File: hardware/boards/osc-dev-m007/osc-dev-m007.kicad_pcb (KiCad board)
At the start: 4 copper layers, 1 part, among them U1 CH32M007E8U7

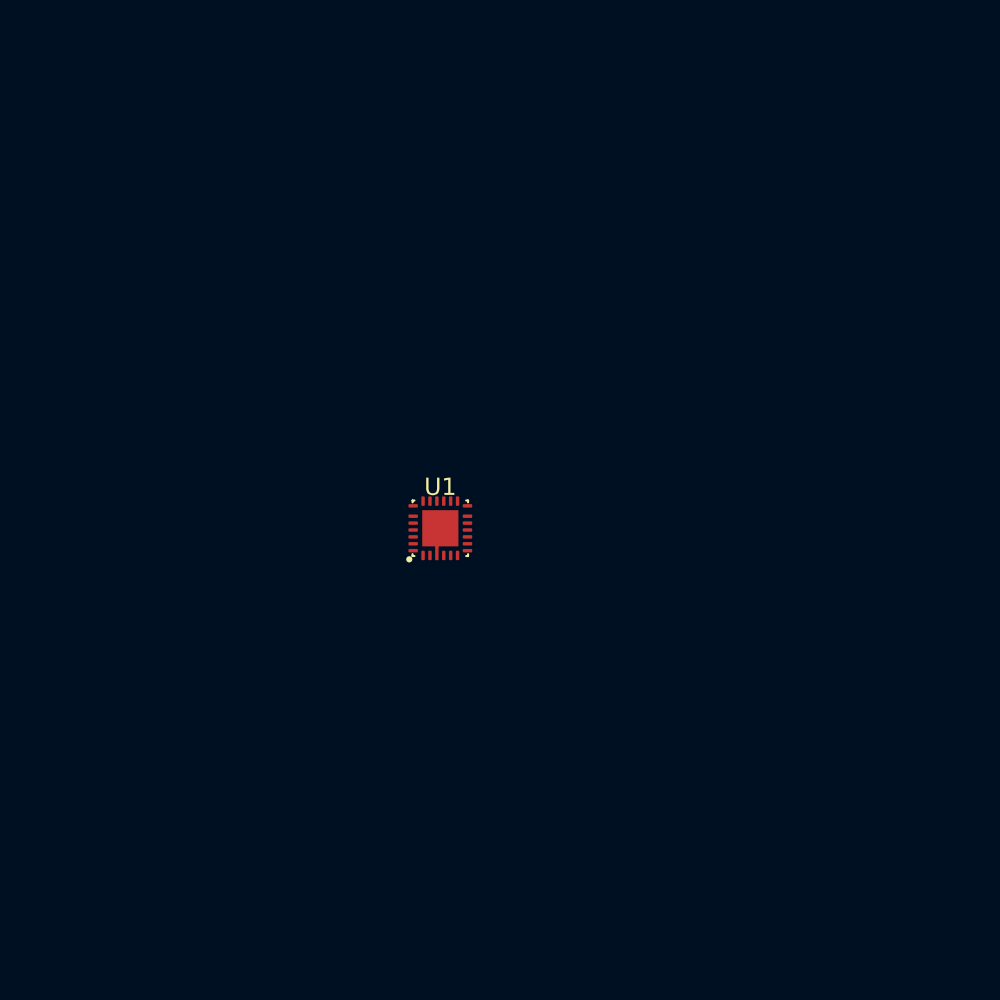
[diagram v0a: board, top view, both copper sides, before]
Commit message: hw: design osc-dev-m007 pcb
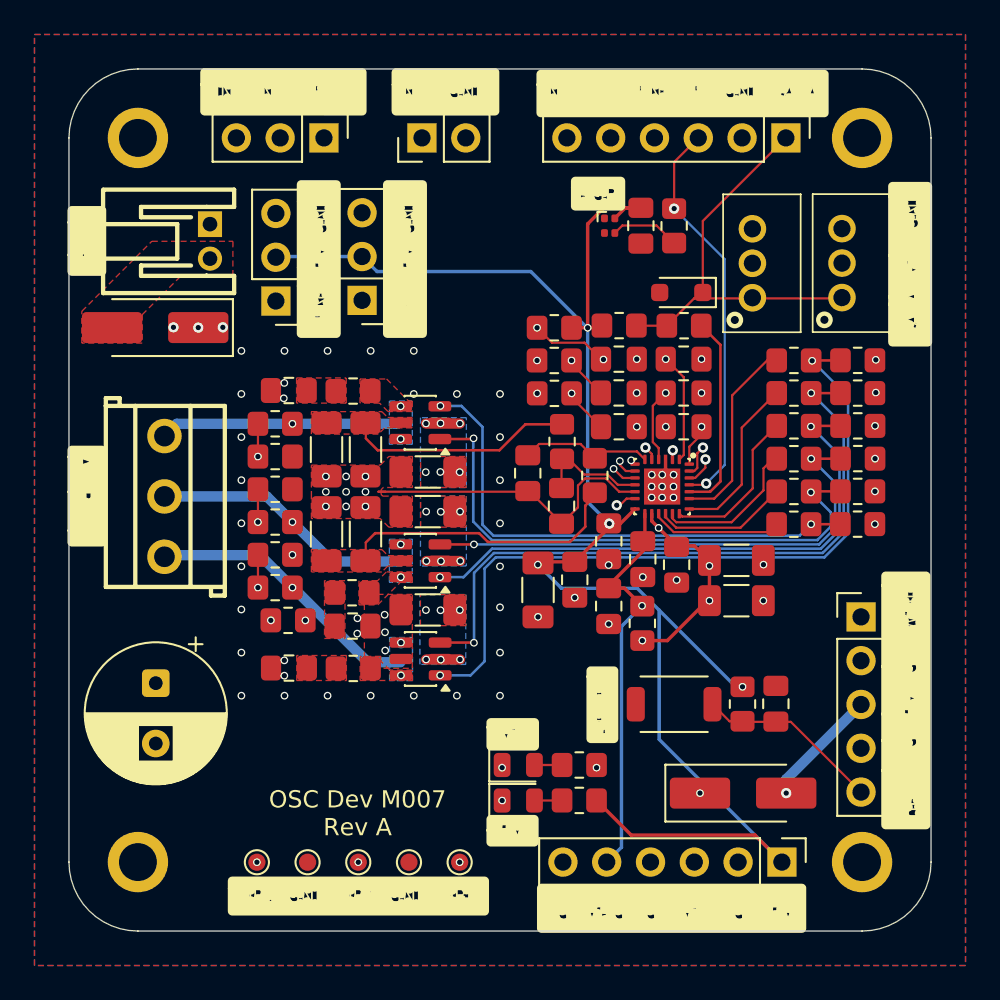
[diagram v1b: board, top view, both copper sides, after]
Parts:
- removed U1: CH32M007E8U7, shared:QFN-26_3x3mm_P0.4mm
- added C1001: 1nF, Capacitor_SMD:C_0805_2012Metric_Pad1.18x1.45mm_HandSolder, F.Cu at (157.0, 98.7)
- added C1002: 0.1µF, Capacitor_SMD:C_0805_2012Metric_Pad1.18x1.45mm_HandSolder, F.Cu at (157.0, 96.7)
- added C1003: 0.1µF, Capacitor_SMD:C_0805_2012Metric_Pad1.18x1.45mm_HandSolder, F.Cu at (157.0, 94.8)
- added C201: 2.2uF, Capacitor_SMD:C_0805_2012Metric_Pad1.18x1.45mm_HandSolder, F.Cu at (156.4, 109.1)
- added C202: 2.2uF, Capacitor_SMD:C_0805_2012Metric_Pad1.18x1.45mm_HandSolder, F.Cu at (158.3, 106.4)
- added C203: 0.1uF, Capacitor_SMD:C_0805_2012Metric_Pad1.18x1.45mm_HandSolder, F.Cu at (160.3, 106.7)
- added C204: 10uF, Capacitor_SMD:C_1206_3216Metric_Pad1.33x1.80mm_HandSolder, F.Cu at (163.8, 106.4)
- added C205: 10uF, Capacitor_SMD:C_1206_3216Metric_Pad1.33x1.80mm_HandSolder, F.Cu at (163.8, 108.8)
- added C206: 0.1uF, Capacitor_SMD:C_0805_2012Metric_Pad1.18x1.45mm_HandSolder, F.Cu at (156.4, 105.3)
- added C207: 1uF, Capacitor_SMD:C_0805_2012Metric_Pad1.18x1.45mm_HandSolder, F.Cu at (154.4, 107.5)
- added C208: 10uF, Capacitor_SMD:C_1206_3216Metric_Pad1.33x1.80mm_HandSolder, F.Cu at (152.3, 108.1)
- added C209: 0.1uF, Capacitor_SMD:C_0805_2012Metric_Pad1.18x1.45mm_HandSolder, F.Cu at (166.1, 114.7)
- added C210: 0.1uF, Capacitor_SMD:C_0805_2012Metric_Pad1.18x1.45mm_HandSolder, F.Cu at (158.2, 87.0)
- added C301: 470uF 25V, Capacitor_THT:CP_Radial_D8.0mm_P3.50mm, F.Cu at (130.1, 113.5)
- added C401: 10uF, Capacitor_SMD:C_1206_3216Metric_Pad1.33x1.80mm_HandSolder, F.Cu at (145.9, 101.3)
- added C402: 1nF, Capacitor_SMD:C_0805_2012Metric_Pad1.18x1.45mm_HandSolder, F.Cu at (160.7, 94.8)
- added C403: 1nF, Capacitor_SMD:C_0805_2012Metric_Pad1.18x1.45mm_HandSolder, F.Cu at (137.8, 96.6)
- added C501: 1nF, Capacitor_SMD:C_0805_2012Metric_Pad1.18x1.45mm_HandSolder, F.Cu at (153.6, 103.3)
- added C601: 10uF, Capacitor_SMD:C_1206_3216Metric_Pad1.33x1.80mm_HandSolder, F.Cu at (145.9, 103.6)
- added C602: 1nF, Capacitor_SMD:C_0805_2012Metric_Pad1.18x1.45mm_HandSolder, F.Cu at (160.7, 96.7)
- added C603: 1nF, Capacitor_SMD:C_0805_2012Metric_Pad1.18x1.45mm_HandSolder, F.Cu at (141.5, 110.2)
- added C701: 1nF, Capacitor_SMD:C_0805_2012Metric_Pad1.18x1.45mm_HandSolder, F.Cu at (151.7, 101.4)
- added C801: 10uF, Capacitor_SMD:C_1206_3216Metric_Pad1.33x1.80mm_HandSolder, F.Cu at (145.9, 109.3)
- added C802: 1nF, Capacitor_SMD:C_0805_2012Metric_Pad1.18x1.45mm_HandSolder, F.Cu at (160.7, 98.7)
- added C803: 1nF, Capacitor_SMD:C_0805_2012Metric_Pad1.18x1.45mm_HandSolder, F.Cu at (137.8, 112.7)
- added D1101: PESD5V0L1BA, Diode_SMD:D_SOD-323_HandSoldering, F.Cu at (160.6, 90.9)
- added D201: STAT, shared:LED_XL-1010RGBC-WS2812B_1x1mm, F.Cu at (156.4, 87.0)
- added D901: SS54, Diode_SMD:D_SMA_Handsoldering, F.Cu at (130.1, 92.9)
- added D902: SS54, Diode_SMD:D_SMA_Handsoldering, F.Cu at (164.2, 119.9)
- added H101: MountingHole_Pad_MP, MountingHole:MountingHole_2.2mm_M2_ISO7380_Pad, F.Cu at (129.1, 81.9)
- added H102: MountingHole_Pad_MP, MountingHole:MountingHole_2.2mm_M2_ISO7380_Pad, F.Cu at (129.1, 123.9)
- added H103: MountingHole_Pad_MP, MountingHole:MountingHole_2.2mm_M2_ISO7380_Pad, F.Cu at (171.1, 123.9)
- added H104: MountingHole_Pad_MP, MountingHole:MountingHole_2.2mm_M2_ISO7380_Pad, F.Cu at (171.1, 81.9)
- added J1001: NTC_EXT, Connector_PinHeader_2.54mm:PinHeader_1x02_P2.54mm_Vertical, F.Cu at (145.5, 81.9)
- added J1002: ENC, Connector_PinHeader_2.54mm:PinHeader_1x03_P2.54mm_Vertical, F.Cu at (137.1, 91.4)
- added J1003: POT, Connector_PinHeader_2.54mm:PinHeader_1x03_P2.54mm_Vertical, F.Cu at (142.1, 91.3)
- added J1101: JST-PH-V, shared:CONN-TH_B3B-PH-K-S, F.Cu at (169.9, 89.2)
- added J1102: JST-PH-V, shared:CONN-TH_B3B-PH-K-S, F.Cu at (164.7, 89.2)
- added J1201: Conn_01x06, Connector_PinHeader_2.54mm:PinHeader_1x06_P2.54mm_Vertical, F.Cu at (166.4, 123.9)
- added J1202: Conn_01x06, Connector_PinHeader_2.54mm:PinHeader_1x06_P2.54mm_Vertical, F.Cu at (166.6, 81.9)
- added J201: PROG, Connector_PinHeader_2.54mm:PinHeader_1x05_P2.54mm_Vertical, F.Cu at (171.0, 109.7)
- added J301: BLDC/BDC(A+B), shared:CONN-TH_3P-P3.50_KF350-3.5-3P, F.Cu at (130.6, 102.7)
- added J901: JST-PH-H, shared:CONN-TH_S2B-PH-K-S-LF-SN, F.Cu at (133.2, 87.9)
- added JP1001: NTC_EXT_INT, Connector_PinHeader_2.54mm:PinHeader_1x03_P2.54mm_Vertical, F.Cu at (139.9, 81.9)
- added LED901: YELLOW, LED_SMD:LED_0805_2012Metric, F.Cu at (151.1, 118.3)
- added LED902: GREEN, LED_SMD:LED_0805_2012Metric, F.Cu at (151.1, 120.4)
- added NT501: NetTie_2, shared:NetTie-2_SMD_0.127mm, F.Cu at (142.3, 99.2)
- added NT502, NT702: NetTie_2, shared:NetTie-2_SMD_0.127mm, F.Cu at (143.2, 102.4)
- added NT701: NetTie_2, shared:NetTie-2_SMD_0.127mm, F.Cu at (142.3, 105.6)
- added Q401: SIL3724A-TP, Package_TO_SOT_SMD:SOT-23-6, F.Cu at (145.4, 98.4)
- added Q601: SIL3724A-TP, Package_TO_SOT_SMD:SOT-23-6, F.Cu at (145.4, 106.5)
- added Q801: SIL3724A-TP, Package_TO_SOT_SMD:SOT-23-6, F.Cu at (145.5, 112.1)
- added R1001: 10kΩ, Resistor_SMD:R_0805_2012Metric_Pad1.20x1.40mm_HandSolder, F.Cu at (153.2, 92.9)
- added R1002: 4.7kΩ, Resistor_SMD:R_0805_2012Metric_Pad1.20x1.40mm_HandSolder, F.Cu at (153.2, 96.7)
- added R1003: 4.7kΩ, Resistor_SMD:R_0805_2012Metric_Pad1.20x1.40mm_HandSolder, F.Cu at (153.2, 94.8)
- added R1101: 33Ω, Resistor_SMD:R_0805_2012Metric_Pad1.20x1.40mm_HandSolder, F.Cu at (160.7, 92.8)
- added R1102: 10kΩ, Resistor_SMD:R_0805_2012Metric_Pad1.20x1.40mm_HandSolder, F.Cu at (157.0, 92.8)
- added R201: 0Ω, Resistor_SMD:R_0805_2012Metric_Pad1.20x1.40mm_HandSolder, F.Cu at (158.3, 110.1)
- added R202: 10KΩ, Resistor_SMD:R_0805_2012Metric_Pad1.20x1.40mm_HandSolder, F.Cu at (164.1, 114.8)
- added R203: 100Ω, Resistor_SMD:R_0805_2012Metric_Pad1.20x1.40mm_HandSolder, F.Cu at (160.2, 87.0)
- added R401: 0, Resistor_SMD:R_0805_2012Metric_Pad1.20x1.40mm_HandSolder, F.Cu at (167.1, 104.3)
- added R402: 0, Resistor_SMD:R_0805_2012Metric_Pad1.20x1.40mm_HandSolder, F.Cu at (167.1, 102.4)
- added R403: 100K, Resistor_SMD:R_0805_2012Metric_Pad1.20x1.40mm_HandSolder, F.Cu at (170.8, 104.3)
- added R404: 100K, Resistor_SMD:R_0805_2012Metric_Pad1.20x1.40mm_HandSolder, F.Cu at (170.8, 102.4)
- added R405: 20K, Resistor_SMD:R_0805_2012Metric_Pad1.20x1.40mm_HandSolder, F.Cu at (137.0, 98.5)
- added R406: 10K, Resistor_SMD:R_0805_2012Metric_Pad1.20x1.40mm_HandSolder, F.Cu at (137.0, 100.4)
- added R407: 10, Resistor_SMD:R_0805_2012Metric_Pad1.20x1.40mm_HandSolder, F.Cu at (141.5, 96.6)
- added R501: 0, Resistor_SMD:R_0805_2012Metric_Pad1.20x1.40mm_HandSolder, F.Cu at (153.7, 99.5)
- added R601: 0, Resistor_SMD:R_0805_2012Metric_Pad1.20x1.40mm_HandSolder, F.Cu at (167.1, 100.5)
- added R602: 0, Resistor_SMD:R_0805_2012Metric_Pad1.20x1.40mm_HandSolder, F.Cu at (167.1, 98.6)
- added R603: 100K, Resistor_SMD:R_0805_2012Metric_Pad1.20x1.40mm_HandSolder, F.Cu at (170.8, 100.5)
- added R604: 100K, Resistor_SMD:R_0805_2012Metric_Pad1.20x1.40mm_HandSolder, F.Cu at (170.8, 98.6)
- added R605: 20K, Resistor_SMD:R_0805_2012Metric_Pad1.20x1.40mm_HandSolder, F.Cu at (137.0, 104.2)
- added R606: 10K, Resistor_SMD:R_0805_2012Metric_Pad1.20x1.40mm_HandSolder, F.Cu at (137.0, 102.3)
- added R607: 10, Resistor_SMD:R_0805_2012Metric_Pad1.20x1.40mm_HandSolder, F.Cu at (141.5, 108.3)
- added R701: 0, Resistor_SMD:R_0805_2012Metric_Pad1.20x1.40mm_HandSolder, F.Cu at (155.6, 101.5)
- added R801: 0, Resistor_SMD:R_0805_2012Metric_Pad1.20x1.40mm_HandSolder, F.Cu at (167.1, 96.7)
- added R802: 0, Resistor_SMD:R_0805_2012Metric_Pad1.20x1.40mm_HandSolder, F.Cu at (167.1, 94.8)
- added R803: 100K, Resistor_SMD:R_0805_2012Metric_Pad1.20x1.40mm_HandSolder, F.Cu at (170.8, 96.7)
- added R804: 100K, Resistor_SMD:R_0805_2012Metric_Pad1.20x1.40mm_HandSolder, F.Cu at (170.8, 94.8)
- added R805: 20K, Resistor_SMD:R_0805_2012Metric_Pad1.20x1.40mm_HandSolder, F.Cu at (137.0, 108.0)
- added R806: 10K, Resistor_SMD:R_0805_2012Metric_Pad1.20x1.40mm_HandSolder, F.Cu at (137.0, 106.1)
- added R807: 10, Resistor_SMD:R_0805_2012Metric_Pad1.20x1.40mm_HandSolder, F.Cu at (141.6, 112.7)
- added R901: 22kΩ, Resistor_SMD:R_0805_2012Metric_Pad1.20x1.40mm_HandSolder, F.Cu at (154.7, 118.3)
- added R902: 10kΩ, Resistor_SMD:R_0805_2012Metric_Pad1.20x1.40mm_HandSolder, F.Cu at (154.7, 120.3)
- added REF**: osc, shared:osc, F.Cu at (141.8, 117.2)
- added R_SH501: 75m, Resistor_SMD:R_1206_3216Metric_Pad1.30x1.75mm_HandSolder, F.Cu at (142.3, 100.0)
- added R_SH502: 150m, Resistor_SMD:R_1206_3216Metric_Pad1.30x1.75mm_HandSolder, F.Cu at (140.0, 100.0)
- added R_SH701: 75m, Resistor_SMD:R_1206_3216Metric_Pad1.30x1.75mm_HandSolder, F.Cu at (142.3, 104.9)
- added R_SH702: 150m, Resistor_SMD:R_1206_3216Metric_Pad1.30x1.75mm_HandSolder, F.Cu at (140.0, 104.9)
- added SW201: RESET, shared:SW_SPST_TS-1088R_3.9x3.0mm, F.Cu at (160.2, 114.8)
- added TH1001: 10kΩ 3950K, Resistor_SMD:R_0805_2012Metric_Pad1.20x1.40mm_HandSolder, F.Cu at (137.8, 109.9)
- added TP1201: TestPoint, TestPoint:TestPoint_Pad_D1.0mm, F.Cu at (147.7, 123.9)
- added TP1202: TestPoint, TestPoint:TestPoint_Pad_D1.0mm, F.Cu at (144.8, 123.9)
- added TP1203: TestPoint, TestPoint:TestPoint_Pad_D1.0mm, F.Cu at (141.8, 123.9)
- added TP1204: TestPoint, TestPoint:TestPoint_Pad_D1.0mm, F.Cu at (138.9, 123.9)
- added TP1205: TestPoint, TestPoint:TestPoint_Pad_D1.0mm, F.Cu at (136.0, 123.9)
- added U201: CH32M007E8U7, shared:QFN-26_3x3mm_P0.4mm, F.Cu at (159.5, 102.1)
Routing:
- net +5V: track 0.00 -> 96.2 mm, vias 0 -> 4
- net NTC: track 0.00 -> 53.7 mm, vias 0 -> 3
- net DBG2: track 0.00 -> 45.8 mm, vias 0 -> 2
- net /BRIDGE/HALFBRIDGE3/G_L: track 0.00 -> 42.8 mm, vias 0 -> 2
- net VSNA: track 0.00 -> 42.7 mm, vias 0 -> 2
- net /BRIDGE/HALFBRIDGE3/G_H: track 0.00 -> 39.1 mm, vias 0 -> 2
- net /MCU/nRST: track 0.00 -> 37.7 mm, vias 0 -> 1
- net VSNB: track 0.00 -> 35.7 mm, vias 0 -> 2
- net VSNC: track 0.00 -> 35.0 mm, vias 0 -> 2
- net DBG0: track 0.00 -> 33.9 mm, vias 0 -> 2
- net /BRIDGE/HALFBRIDGE2/G_L: track 0.00 -> 32.8 mm, vias 0 -> 2
- net /BRIDGE/HALFBRIDGE1/G_L: track 0.00 -> 32.6 mm, vias 0 -> 2
- net /MCU/SWDIO: track 0.00 -> 32.4 mm, vias 0 -> 1
- net /BRIDGE/HALFBRIDGE1/G_H: track 0.00 -> 30.0 mm, vias 0 -> 2
- net /BRIDGE/HALFBRIDGE2/G_H: track 0.00 -> 29.7 mm, vias 0 -> 2
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- added copper zone on F.Cu, net /BRIDGE/HALFBRIDGE1/LEG
- added copper zone on F.Cu, net /BRIDGE/HALFBRIDGE1/SNUB
- added copper zone on F.Cu, net /BRIDGE/HALFBRIDGE2/LEG
- added copper zone on F.Cu, net /BRIDGE/HALFBRIDGE2/SNUB
- added copper zone on F.Cu, net /BRIDGE/HALFBRIDGE3/SNUB
- added copper zone on B.Cu, net /BRIDGE/PH_A
- added copper zone on F.Cu, net /BRIDGE/PH_A
- added copper zone on B.Cu, net /BRIDGE/PH_B
- added copper zone on F.Cu, net /BRIDGE/PH_B
- added copper zone on B.Cu, net /BRIDGE/PH_C
- added copper zone on F.Cu, net /BRIDGE/PH_C
- added copper zone on B.Cu, net GND
- added copper zone on F.Cu, net GND
- added copper zone on In1.Cu, net GND
- added copper zone on In2.Cu, net GND
- added copper zone on In4.Cu, net GND
- added copper zone on F.Cu, net VBAT
- added copper zone on B.Cu, net VSYS
- added copper zone on F.Cu, net VSYS
- added copper zone on In3.Cu, net VSYS
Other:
- board outline added: 50 x 50 mm
- copper layers 4 -> 6
- board text added: "- +"
- board text added: "5V"
- board text added: "6.5-15V"
- board text added: "A B C"
- board text added: "BDC A+B"
- board text added: "DATA"
- board text added: "DB0"
- board text added: "DB1"
- board text added: "DB2"
- board text added: "ENC"
- board text added: "EXT"
- board text added: "G"
- board text added: "GND"
- board text added: "INT"
- board text added: "LED"
- board text added: "NTC"
- board text added: "OSC Dev M007 Rev A"
- board text added: "OSC Dev M007 Rev. A"
- board text added: "POS"
- board text added: "POT"
- board text added: "RESET"
- board text added: "RGB"
- board text added: "SWDIO"
- board text added: "VRG"
- board text added: "VS"
- board text added: "nRST"

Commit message: hw: add osc-sg90-m007 renders to readme
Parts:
- C1002, C1003: value 0.1µF -> 0.1uF
- R1001, R1102, R902: value 10kΩ -> 10k
- R1002, R1003: value 4.7kΩ -> 4.7k
- R1101: value 33Ω -> 33
- R201: value 0Ω -> 0
- R202: value 10KΩ -> 10k
- R203: value 100Ω -> 100
- R403, R404, R603, R604, R803, R804: value 100K -> 100k
- R405, R605, R805: value 20K -> 20k
- R406, R606, R806: value 10K -> 10k
- R901: value 22kΩ -> 22k
- TH1001: value 10kΩ 3950K -> 10k 3950K
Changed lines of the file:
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@@
 			)
 		)
-		(property "Value" "100K"
+		(property "Value" "100k"
 			(at 0 1.65 0)
 			(layer "F.Fab")
@@
 		(sheetname "/POWER/")
 		(sheetfile "power.kicad_sch")
+		(units
+			(unit
+				(name "A")
+				(pins "1" "2")
+			)
+		)
 		(attr through_hole)
 		(duplicate_pad_numbers_are_jumpers no)
@@
 			)
 		)
-		(property "Value" "0.1µF"
+		(property "Value" "0.1uF"
 			(at 0 1.68 0)
 			(layer "F.Fab")
@@
 			)
 		)
-		(property "Value" "4.7kΩ"
+		(property "Value" "4.7k"
 			(at 0 1.65 0)
 			(layer "F.Fab")
@@
 			)
 		)
-		(property "Value" "10kΩ 3950K"
+		(property "Value" "10k 3950K"
 			(at 0 1.65 0)
 			(layer "F.Fab")
@@
 			)
 		)
-		(property "Value" "100Ω"
+		(property "Value" "100"
 			(at 0 1.65 90)
 			(layer "F.Fab")
@@
 			)
 		)
-		(property "Value" "10kΩ"
+		(property "Value" "10k"
 			(at 0 1.65 0)
 			(layer "F.Fab")
@@
 			)
 		)
-		(property "Value" "10K"
+		(property "Value" "10k"
 			(at 0 1.65 0)
 			(layer "F.Fab")
@@
 			)
 		)
-		(property "Value" "22kΩ"
+		(property "Value" "22k"
 			(at 0 1.65 0)
 			(layer "F.Fab")
@@
 			)
 		)
-		(property "Value" "10kΩ"
+		(property "Value" "10k"
 			(at 0 1.65 0)
 			(layer "F.Fab")
@@
 			)
 		)
-		(property "Value" "10kΩ"
+		(property "Value" "10k"
 			(at 0 1.65 0)
 			(layer "F.Fab")
@@
 			)
 		)
-		(property "Value" "4.7kΩ"
+		(property "Value" "4.7k"
 			(at 0 1.65 0)
 			(layer "F.Fab")
@@
 			)
 		)
-		(property "Value" "100K"
+		(property "Value" "100k"
 			(at 0 1.65 0)
 			(layer "F.Fab")
@@
 			)
 		)
-		(property "Value" "33Ω"
+		(property "Value" "33"
 			(at 0 1.65 0)
 			(layer "F.Fab")
@@
 			)
 		)
-		(property "Value" "0.1µF"
+		(property "Value" "0.1uF"
 			(at 0 1.68 0)
 			(layer "F.Fab")
@@
 			)
 		)
-		(property "Value" "0Ω"
+		(property "Value" "0"
 			(at 0 1.65 90)
 			(layer "F.Fab")
@@
 			)
 		)
-		(property "Value" "10K"
+		(property "Value" "10k"
 			(at 0 1.65 0)
 			(layer "F.Fab")
@@
 			)
 		)
-		(property "Value" "10K"
+		(property "Value" "10k"
 			(at 0 1.65 0)
 			(layer "F.Fab")
@@
 			)
 		)
-		(property "Value" "100K"
+		(property "Value" "100k"
 			(at 0.5 2.06 0)
 			(layer "F.Fab")
@@
 			)
 		)
-		(property "Value" "100K"
+		(property "Value" "100k"
 			(at 0 1.65 0)
 			(layer "F.Fab")
@@
 			)
 		)
-		(property "Value" "20K"
+		(property "Value" "20k"
 			(at 0 1.65 0)
 			(layer "F.Fab")
@@
 			)
 		)
-		(property "Value" "100K"
+		(property "Value" "100k"
 			(at 0 1.65 0)
 			(layer "F.Fab")
@@
 			)
 		)
-		(property "Value" "100K"
+		(property "Value" "100k"
 			(at -6 -10.35 0)
 			(layer "F.Fab")
@@
 			)
 		)
-		(property "Value" "20K"
+		(property "Value" "20k"
 			(at 0 1.65 0)
 			(layer "F.Fab")
@@
 			)
 		)
-		(property "Value" "10KΩ"
+		(property "Value" "10k"
 			(at 0 1.65 90)
 			(layer "F.Fab")
@@
 			)
 		)
-		(property "Value" "20K"
+		(property "Value" "20k"
 			(at 0 1.65 0)
 			(layer "F.Fab")

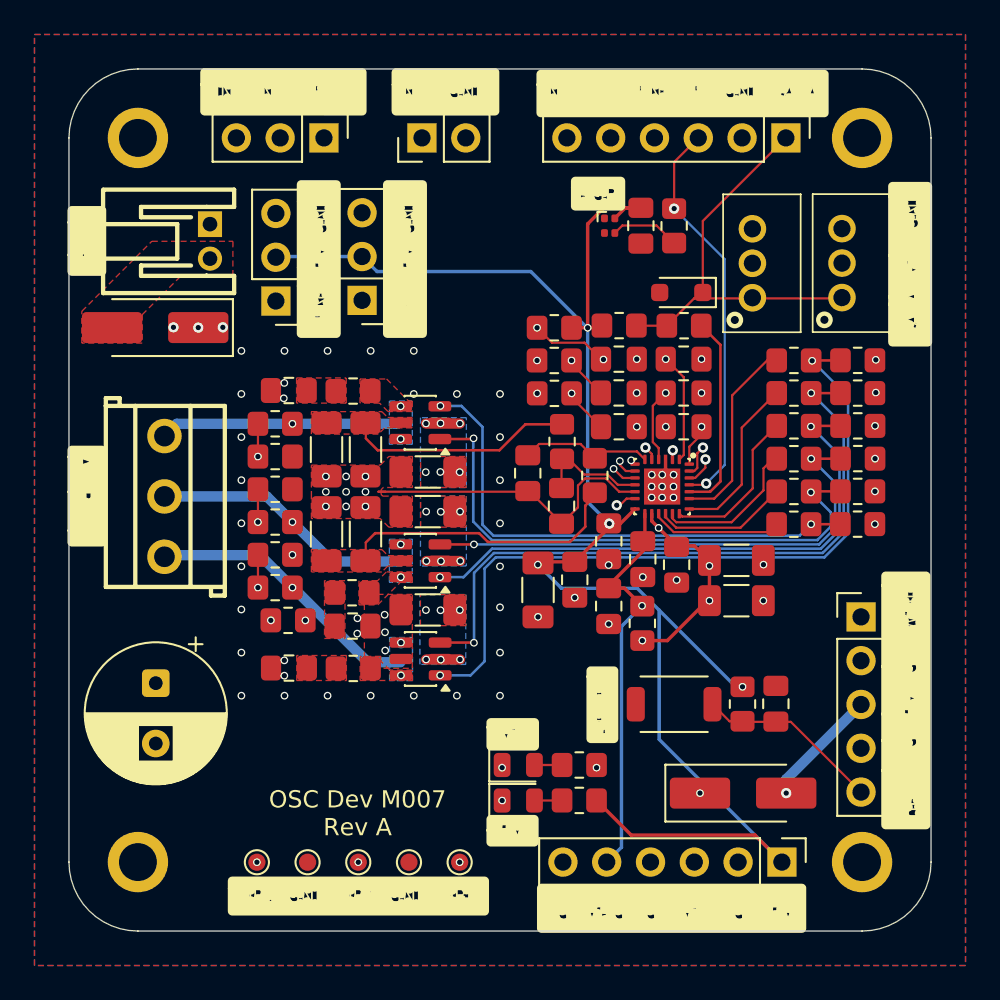
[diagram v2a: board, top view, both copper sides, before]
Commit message: hw: swap dev-m007 parts to in-stock equivalents
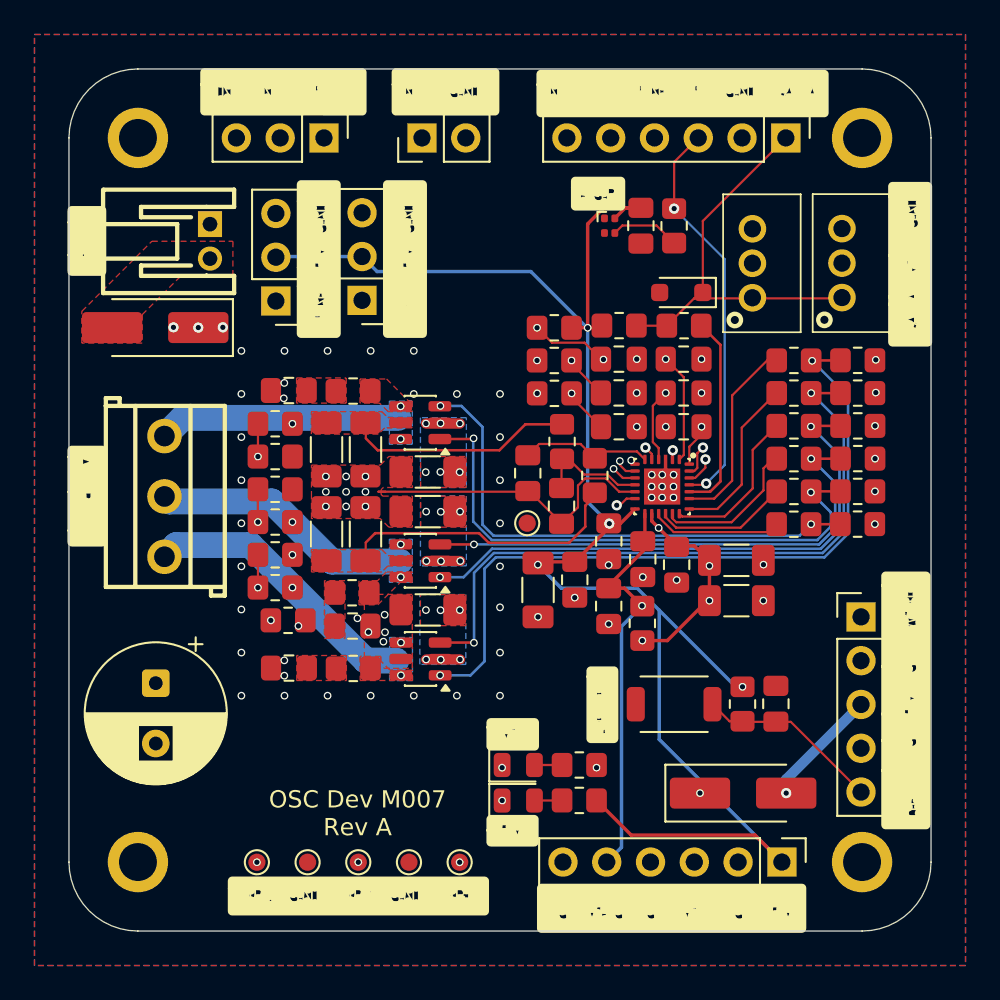
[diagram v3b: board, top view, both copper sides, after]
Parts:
- added TP1206: TestPoint, TestPoint:TestPoint_Pad_D1.0mm, F.Cu at (151.6, 104.3)
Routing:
- net GATE_AH: track 7.59 -> 6.74 mm
- net ISNS2+: track 7.76 -> 7.20 mm
